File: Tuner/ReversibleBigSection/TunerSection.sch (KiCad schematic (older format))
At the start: 112 parts, among them J1 Conn_01x03, J10 Conn_01x02, J11 Conn_02x05_Odd_Even, J12 Conn_01x01, J13 Conn_01x01, J14 Conn_01x01, J15 Conn_01x01, J2 Conn_01x03, J3 Conn_01x03, J4 Conn_01x03, J5 Conn_01x03, J6 Conn_01x03, J7 Conn_01x03, J8 Conn_01x02, J9 Conn_01x02, P10 Conn_01x01, P11 Conn_01x01, P12 Conn_01x01, P2 Conn_01x01, P3 Conn_01x01, P4 Conn_01x01, P5 Conn_01x01, P6 Conn_01x01, P7 Conn_01x01, P8 Conn_01x01, P9 Conn_01x01, U1 MCP23008, U2 ULN2803A

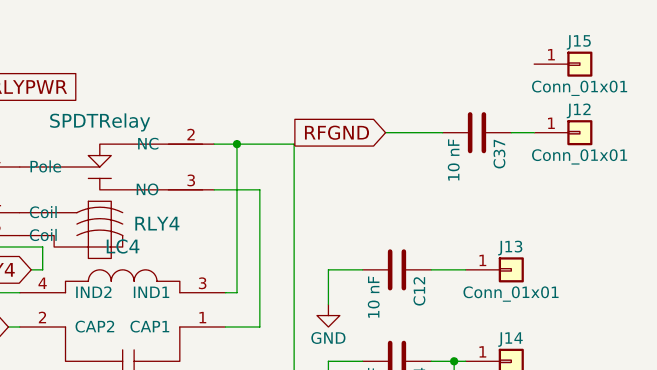
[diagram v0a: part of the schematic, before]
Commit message: Added HK19F boards
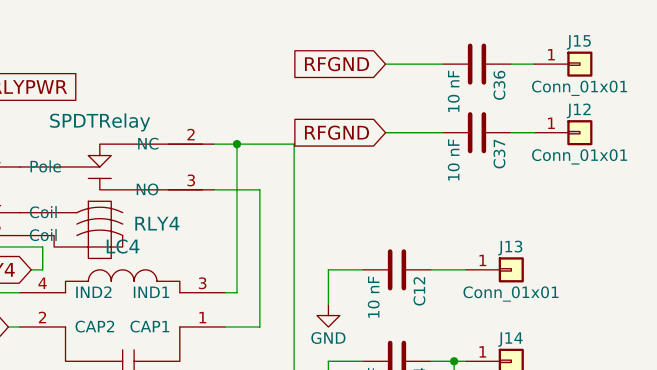
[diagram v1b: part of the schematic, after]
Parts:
- added C36: 10 nF, Capacitors_THT:C_Disc_D5.0mm_W2.5mm_P5.00mm, symbol C
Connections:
- net RFGND: now also C36.2
- net at J15.1 (Pin_1): now also C36.1
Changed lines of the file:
@@
 RLY8
 $Comp
-L +5V #PWR01
+L +5V #PWR13
 U 1 1 5B1A0287
 P 3150 5750
-F 0 "#PWR01" H 3150 5600 50  0001 C CNN
+F 0 "#PWR13" H 3150 5600 50  0001 C CNN
 F 1 "+5V" H 3150 5890 50  0000 C CNN
 F 2 "" H 3150 5750 50  0001 C CNN
@@
 $EndComp
 $Comp
-L GND #PWR02
+L GND #PWR3
 U 1 1 5B1AA0F6
 P 900 4500
-F 0 "#PWR02" H 900 4250 50  0001 C CNN
+F 0 "#PWR3" H 900 4250 50  0001 C CNN
 F 1 "GND" H 900 4350 50  0000 C CNN
 F 2 "" H 900 4500 50  0001 C CNN
@@
 $EndComp
 $Comp
-L +5V #PWR03
+L +5V #PWR2
 U 1 1 5B1AABE9
 P 900 3750
-F 0 "#PWR03" H 900 3600 50  0001 C CNN
+F 0 "#PWR2" H 900 3600 50  0001 C CNN
 F 1 "+5V" H 900 3890 50  0000 C CNN
 F 2 "" H 900 3750 50  0001 C CNN
@@
 $EndComp
 $Comp
-L +5V #PWR04
+L +5V #PWR9
 U 1 1 5B1ABA5A
 P 2150 4450
-F 0 "#PWR04" H 2150 4300 50  0001 C CNN
+F 0 "#PWR9" H 2150 4300 50  0001 C CNN
 F 1 "+5V" H 2150 4590 50  0000 C CNN
 F 2 "" H 2150 4450 50  0001 C CNN
@@
 $EndComp
 $Comp
-L +5V #PWR05
+L +5V #PWR11
 U 1 1 5B1ABCDE
 P 2400 3950
-F 0 "#PWR05" H 2400 3800 50  0001 C CNN
+F 0 "#PWR11" H 2400 3800 50  0001 C CNN
 F 1 "+5V" H 2400 4090 50  0000 C CNN
 F 2 "" H 2400 3950 50  0001 C CNN
@@
 $EndComp
 $Comp
-L +5V #PWR06
+L +5V #PWR17
 U 1 1 5B1ABFC6
 P 8800 4600
-F 0 "#PWR06" H 8800 4450 50  0001 C CNN
+F 0 "#PWR17" H 8800 4450 50  0001 C CNN
 F 1 "+5V" H 8800 4740 50  0000 C CNN
 F 2 "" H 8800 4600 50  0001 C CNN
@@
 $EndComp
 $Comp
-L GND #PWR07
+L GND #PWR18
 U 1 1 5B1AC04C
 P 8800 5050
-F 0 "#PWR07" H 8800 4800 50  0001 C CNN
+F 0 "#PWR18" H 8800 4800 50  0001 C CNN
 F 1 "GND" H 8800 4900 50  0000 C CNN
 F 2 "" H 8800 5050 50  0001 C CNN
@@
 $EndComp
 $Comp
-L +5V #PWR08
+L +5V #PWR10
 U 1 1 5B196BCE
 P 2250 3950
-F 0 "#PWR08" H 2250 3800 50  0001 C CNN
+F 0 "#PWR10" H 2250 3800 50  0001 C CNN
 F 1 "+5V" H 2250 4090 50  0000 C CNN
 F 2 "" H 2250 3950 50  0001 C CNN
@@
 $EndComp
 $Comp
-L GND #PWR09
+L GND #PWR15
 U 1 1 5B9A4AE1
 P 4850 6650
-F 0 "#PWR09" H 4850 6400 50  0001 C CNN
+F 0 "#PWR15" H 4850 6400 50  0001 C CNN
 F 1 "GND" H 4850 6500 50  0000 C CNN
 F 2 "" H 4850 6650 50  0001 C CNN
@@
 $EndComp
 $Comp
-L GND #PWR010
+L GND #PWR12
 U 1 1 5B9A6036
 P 3150 4200
-F 0 "#PWR010" H 3150 3950 50  0001 C CNN
+F 0 "#PWR12" H 3150 3950 50  0001 C CNN
 F 1 "GND" H 3150 4050 50  0000 C CNN
 F 2 "" H 3150 4200 50  0001 C CNN
@@
 $EndComp
 $Comp
-L GND #PWR011
+L GND #PWR14
 U 1 1 5B9ACA36
 P 3550 6100
-F 0 "#PWR011" H 3550 5850 50  0001 C CNN
+F 0 "#PWR14" H 3550 5850 50  0001 C CNN
 F 1 "GND" H 3550 5950 50  0000 C CNN
 F 2 "" H 3550 6100 50  0001 C CNN
@@
 $EndComp
 $Comp
-L GND #PWR012
+L GND #PWR19
 U 1 1 5B982525
 P 9850 2000
-F 0 "#PWR012" H 9850 1750 50  0001 C CNN
+F 0 "#PWR19" H 9850 1750 50  0001 C CNN
 F 1 "GND" H 9850 1850 50  0000 C CNN
 F 2 "" H 9850 2000 50  0001 C CNN
@@
 $EndComp
 $Comp
-L GND #PWR013
+L GND #PWR7
 U 1 1 5BA4D8F3
 P 1800 5850
-F 0 "#PWR013" H 1800 5600 50  0001 C CNN
+F 0 "#PWR7" H 1800 5600 50  0001 C CNN
 F 1 "GND" H 1800 5700 50  0000 C CNN
 F 2 "" H 1800 5850 50  0001 C CNN
@@
 $EndComp
 $Comp
-L +5V #PWR014
+L +5V #PWR8
 U 1 1 5BA4E273
 P 1850 5300
-F 0 "#PWR014" H 1850 5150 50  0001 C CNN
+F 0 "#PWR8" H 1850 5150 50  0001 C CNN
 F 1 "+5V" H 1850 5440 50  0000 C CNN
 F 2 "" H 1850 5300 50  0001 C CNN
@@
 $EndComp
 $Comp
-L +5V #PWR015
+L +5V #PWR6
 U 1 1 5BA4E663
 P 1200 5700
-F 0 "#PWR015" H 1200 5550 50  0001 C CNN
+F 0 "#PWR6" H 1200 5550 50  0001 C CNN
 F 1 "+5V" H 1200 5840 50  0000 C CNN
 F 2 "" H 1200 5700 50  0001 C CNN
@@
 $EndComp
 $Comp
-L GND #PWR016
+L GND #PWR1
 U 1 1 5BA4FB25
 P 750 5900
-F 0 "#PWR016" H 750 5650 50  0001 C CNN
+F 0 "#PWR1" H 750 5650 50  0001 C CNN
 F 1 "GND" H 750 5750 50  0000 C CNN
 F 2 "" H 750 5900 50  0001 C CNN
@@
 $EndComp
 $Comp
-L GND #PWR017
+L GND #PWR5
 U 1 1 5BA5005D
 P 1100 5300
-F 0 "#PWR017" H 1100 5050 50  0001 C CNN
+F 0 "#PWR5" H 1100 5050 50  0001 C CNN
 F 1 "GND" H 1100 5150 50  0000 C CNN
 F 2 "" H 1100 5300 50  0001 C CNN
@@
 EXTPWR
 $Comp
-L +5V #PWR018
+L +5V #PWR4
 U 1 1 5BAE4DBC
 P 1000 4850
-F 0 "#PWR018" H 1000 4700 50  0001 C CNN
+F 0 "#PWR4" H 1000 4700 50  0001 C CNN
 F 1 "+5V" H 1000 4990 50  0000 C CNN
 F 2 "" H 1000 4850 50  0001 C CNN
@@
 	700  4850 1000 4850
 $Comp
-L GND #PWR019
+L GND #PWR16
 U 1 1 5BAEE216
 P 5050 7250
-F 0 "#PWR019" H 5050 7000 50  0001 C CNN
+F 0 "#PWR16" H 5050 7000 50  0001 C CNN
 F 1 "GND" H 5050 7100 50  0000 C CNN
 F 2 "" H 5050 7250 50  0001 C CNN
@@
 Wire Wire Line
 	10100 1250 10350 1250
+$Comp
+L C C36
+U 1 1 5BCFC27C
+P 10500 950
+F 0 "C36" H 10525 1050 50  0000 L CNN
+F 1 "10 nF" H 10525 850 50  0000 L CNN
+F 2 "Capacitors_THT:C_Disc_D5.0mm_W2.5mm_P5.00mm" H 10538 800 50  0001 C CNN
+F 3 "" H 10500 950 50  0001 C CNN
+	1    10500 950
+	0    1    1    0
+$EndComp
+Text GLabel 10100 950  0    60   Input ~ 0
+RFGND
+Wire Wire Line
+	10100 950  10350 950
+Wire Wire Line
+	10650 950  10750 950
 $EndSCHEMATC

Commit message: JLCPCB Nov 1 2018
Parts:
- removed C36, C37: 10 nF, Capacitors_THT:C_Disc_D5.0mm_W2.5mm_P5.00mm, symbol C
- added J16, J17, J18, J19, J20, J21, J22: Conn_01x01, tuner:SOLDERJUMPER, symbol Conn_01x01
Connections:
- net RFGND: now also J17.1 (Pin_1)
- net at J9.2 (Pin_2), RLY9.2 (NC): now also J16.1 (Pin_1)
- net at J10.2 (Pin_2), RLY9.3 (NO): now also J22.1 (Pin_1)
- net at J15.1 (Pin_1): now also J18.1 (Pin_1), J19.1 (Pin_1)
- net at J12.1 (Pin_1): now also J20.1 (Pin_1), J21.1 (Pin_1)
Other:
- moved on the sheet: J12, J15
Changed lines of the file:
@@
 L Conn_01x01 J15
 U 1 1 5B19812D
-P 10950 950
-F 0 "J15" H 10950 1050 50  0000 C CNN
-F 1 "Conn_01x01" H 10950 850 50  0000 C CNN
-F 2 "Connectors:1pin" H 10950 950 50  0001 C CNN
-F 3 "" H 10950 950 50  0001 C CNN
-	1    10950 950
+P 11100 600
+F 0 "J15" H 11100 700 50  0000 C CNN
+F 1 "Conn_01x01" H 11100 500 50  0000 C CNN
+F 2 "Connectors:1pin" H 11100 600 50  0001 C CNN
+F 3 "" H 11100 600 50  0001 C CNN
+	1    11100 600
 	1    0    0    -1
 $EndComp
@@
 L Conn_01x01 J12
 U 1 1 5B1981D8
-P 10950 1250
-F 0 "J12" H 10950 1350 50  0000 C CNN
-F 1 "Conn_01x01" H 10950 1150 50  0000 C CNN
-F 2 "Connectors:1pin" H 10950 1250 50  0001 C CNN
-F 3 "" H 10950 1250 50  0001 C CNN
-	1    10950 1250
+P 11100 850
+F 0 "J12" H 11100 950 50  0000 C CNN
+F 1 "Conn_01x01" H 11100 750 50  0000 C CNN
+F 2 "Connectors:1pin" H 11100 850 50  0001 C CNN
+F 3 "" H 11100 850 50  0001 C CNN
+	1    11100 850
 	1    0    0    -1
 $EndComp
@@
 	-1   0    0    1
 $EndComp
+$Comp
+L GND #PWR16
+U 1 1 5BAEE216
+P 5050 7250
+F 0 "#PWR16" H 5050 7000 50  0001 C CNN
+F 1 "GND" H 5050 7100 50  0000 C CNN
+F 2 "" H 5050 7250 50  0001 C CNN
+F 3 "" H 5050 7250 50  0001 C CNN
+	1    5050 7250
+	1    0    0    -1
+$EndComp
+$Comp
+L C C34
+U 1 1 5BC6B88C
+P 5050 6000
+F 0 "C34" H 5075 6100 50  0000 L CNN
+F 1 "10 nF" H 5075 5900 50  0000 L CNN
+F 2 "Capacitors_THT:C_Disc_D5.0mm_W2.5mm_P5.00mm" H 5088 5850 50  0001 C CNN
+F 3 "" H 5050 6000 50  0001 C CNN
+	1    5050 6000
+	0    1    1    0
+$EndComp
+$Comp
+L C C35
+U 1 1 5BC6CF6F
+P 10150 2550
+F 0 "C35" H 10175 2650 50  0000 L CNN
+F 1 "10 nF" H 10175 2450 50  0000 L CNN
+F 2 "Capacitors_THT:C_Disc_D5.0mm_W2.5mm_P5.00mm" H 10188 2400 50  0001 C CNN
+F 3 "" H 10150 2550 50  0001 C CNN
+	1    10150 2550
+	0    1    1    0
+$EndComp
+Text GLabel 9600 650  0    60   Input ~ 0
+RFGND
+$Comp
+L Conn_01x01 J17
+U 1 1 5BD84E29
+P 9950 650
+F 0 "J17" H 9950 750 50  0000 C CNN
+F 1 "Conn_01x01" H 9950 550 50  0000 C CNN
+F 2 "tuner:SOLDERJUMPER" H 9950 650 50  0001 C CNN
+F 3 "" H 9950 650 50  0001 C CNN
+	1    9950 650
+	1    0    0    -1
+$EndComp
 Connection ~ 10200 5350
 Wire Wire Line
@@
 	10150 4150 10150 3700
 Wire Wire Line
-	9600 4150 10150 4150
+	9600 4150 10350 4150
 Wire Wire Line
 	9900 3200 10150 3200
@@
 Wire Wire Line
 	700  4850 1000 4850
-$Comp
-L GND #PWR16
-U 1 1 5BAEE216
-P 5050 7250
-F 0 "#PWR16" H 5050 7000 50  0001 C CNN
-F 1 "GND" H 5050 7100 50  0000 C CNN
-F 2 "" H 5050 7250 50  0001 C CNN
-F 3 "" H 5050 7250 50  0001 C CNN
-	1    5050 7250
-	1    0    0    -1
-$EndComp
 Wire Wire Line
 	5050 7200 5050 7250
@@
 	5050 6600 5250 6600
 Connection ~ 5250 6600
-$Comp
-L C C34
-U 1 1 5BC6B88C
-P 5050 6000
-F 0 "C34" H 5075 6100 50  0000 L CNN
-F 1 "10 nF" H 5075 5900 50  0000 L CNN
-F 2 "Capacitors_THT:C_Disc_D5.0mm_W2.5mm_P5.00mm" H 5088 5850 50  0001 C CNN
-F 3 "" H 5050 6000 50  0001 C CNN
-	1    5050 6000
-	0    1    1    0
-$EndComp
 Wire Wire Line
 	4700 6000 4900 6000
@@
 	5250 6000 5200 6000
 Connection ~ 5250 6000
-$Comp
-L C C35
-U 1 1 5BC6CF6F
-P 10150 2550
-F 0 "C35" H 10175 2650 50  0000 L CNN
-F 1 "10 nF" H 10175 2450 50  0000 L CNN
-F 2 "Capacitors_THT:C_Disc_D5.0mm_W2.5mm_P5.00mm" H 10188 2400 50  0001 C CNN
-F 3 "" H 10150 2550 50  0001 C CNN
-	1    10150 2550
-	0    1    1    0
-$EndComp
 Wire Wire Line
 	9850 2550 10000 2550
@@
 	10400 2550 10400 2250
 Connection ~ 10400 2250
-Text GLabel 10100 1250 0    60   Input ~ 0
-RFGND
-$Comp
-L C C37
-U 1 1 5BCC2C84
-P 10500 1250
-F 0 "C37" H 10525 1350 50  0000 L CNN
-F 1 "10 nF" H 10525 1150 50  0000 L CNN
-F 2 "Capacitors_THT:C_Disc_D5.0mm_W2.5mm_P5.00mm" H 10538 1100 50  0001 C CNN
-F 3 "" H 10500 1250 50  0001 C CNN
-	1    10500 1250
-	0    1    1    0
-$EndComp
-Wire Wire Line
-	10650 1250 10750 1250
-Wire Wire Line
-	10100 1250 10350 1250
-$Comp
-L C C36
-U 1 1 5BCFC27C
-P 10500 950
-F 0 "C36" H 10525 1050 50  0000 L CNN
-F 1 "10 nF" H 10525 850 50  0000 L CNN
-F 2 "Capacitors_THT:C_Disc_D5.0mm_W2.5mm_P5.00mm" H 10538 800 50  0001 C CNN
-F 3 "" H 10500 950 50  0001 C CNN
-	1    10500 950
-	0    1    1    0
-$EndComp
-Text GLabel 10100 950  0    60   Input ~ 0
-RFGND
-Wire Wire Line
-	10100 950  10350 950
-Wire Wire Line
-	10650 950  10750 950
+Wire Wire Line
+	9750 650  9600 650
+$Comp
+L Conn_01x01 J18
+U 1 1 5BD85A19
+P 10550 550
+F 0 "J18" H 10550 650 50  0000 C CNN
+F 1 "Conn_01x01" H 10550 450 50  0000 C CNN
+F 2 "tuner:SOLDERJUMPER" H 10550 550 50  0001 C CNN
+F 3 "" H 10550 550 50  0001 C CNN
+	1    10550 550
+	-1   0    0    1
+$EndComp
+$Comp
+L Conn_01x01 J19
+U 1 1 5BD85C02
+P 10550 650
+F 0 "J19" H 10550 750 50  0000 C CNN
+F 1 "Conn_01x01" H 10550 550 50  0000 C CNN
+F 2 "tuner:SOLDERJUMPER" H 10550 650 50  0001 C CNN
+F 3 "" H 10550 650 50  0001 C CNN
+	1    10550 650
+	-1   0    0    1
+$EndComp
+Wire Wire Line
+	10750 550  10750 650
+Wire Wire Line
+	10750 600  10900 600
+Connection ~ 10750 600
+$Comp
+L Conn_01x01 J20
+U 1 1 5BD861F6
+P 10550 850
+F 0 "J20" H 10550 950 50  0000 C CNN
+F 1 "Conn_01x01" H 10550 750 50  0000 C CNN
+F 2 "tuner:SOLDERJUMPER" H 10550 850 50  0001 C CNN
+F 3 "" H 10550 850 50  0001 C CNN
+	1    10550 850
+	-1   0    0    1
+$EndComp
+$Comp
+L Conn_01x01 J21
+U 1 1 5BD86365
+P 10550 950
+F 0 "J21" H 10550 1050 50  0000 C CNN
+F 1 "Conn_01x01" H 10550 850 50  0000 C CNN
+F 2 "tuner:SOLDERJUMPER" H 10550 950 50  0001 C CNN
+F 3 "" H 10550 950 50  0001 C CNN
+	1    10550 950
+	-1   0    0    1
+$EndComp
+Wire Wire Line
+	10750 850  10750 950
+Wire Wire Line
+	10900 850  10900 900
+Wire Wire Line
+	10900 900  10750 900
+Connection ~ 10750 900
+$Comp
+L Conn_01x01 J22
+U 1 1 5BD86A55
+P 10550 4150
+F 0 "J22" H 10550 4250 50  0000 C CNN
+F 1 "Conn_01x01" H 10550 4050 50  0000 C CNN
+F 2 "tuner:SOLDERJUMPER" H 10550 4150 50  0001 C CNN
+F 3 "" H 10550 4150 50  0001 C CNN
+	1    10550 4150
+	1    0    0    -1
+$EndComp
+Connection ~ 10150 4150
+$Comp
+L Conn_01x01 J16
+U 1 1 5BD872C1
+P 9550 3750
+F 0 "J16" H 9550 3850 50  0000 C CNN
+F 1 "Conn_01x01" H 9550 3650 50  0000 C CNN
+F 2 "tuner:SOLDERJUMPER" H 9550 3750 50  0001 C CNN
+F 3 "" H 9550 3750 50  0001 C CNN
+	1    9550 3750
+	-1   0    0    1
+$EndComp
+Wire Wire Line
+	9750 3750 9900 3750
+Connection ~ 9900 3750
 $EndSCHEMATC

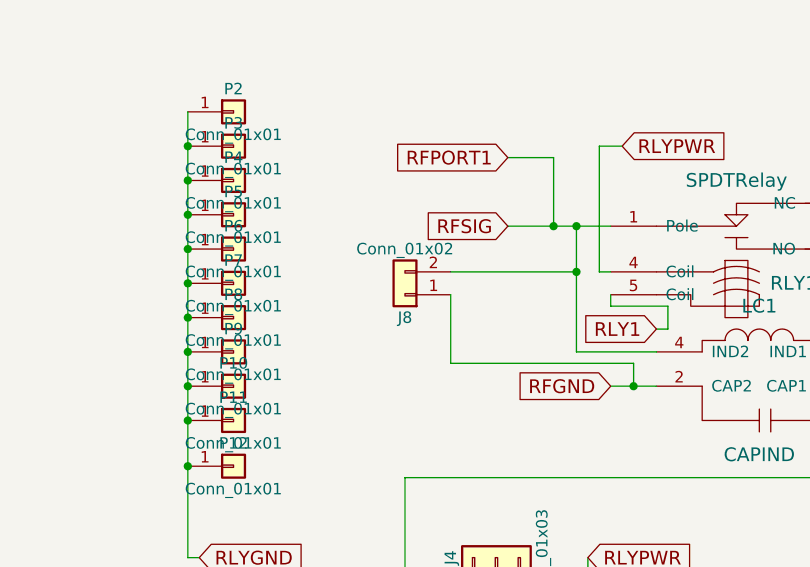
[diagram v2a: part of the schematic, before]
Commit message: Modified connectors on Reversible boards
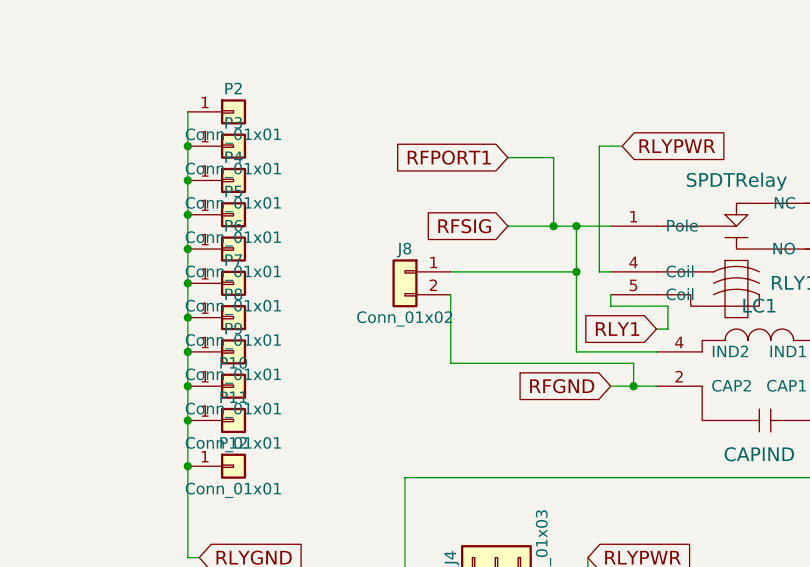
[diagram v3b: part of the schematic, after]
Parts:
- J10, J8, J9: footprint Connectors_Terminal_Blocks:TerminalBlock_bornier-2_P5.08mm -> tuner:bnc_90_1-1337543-0_pad_combo
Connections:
- net RFGND: now also J8.2 (Pin_2); no longer J8.1 (Pin_1)
- net RFPORT1: now also J8.1 (Pin_1); no longer J8.2 (Pin_2)
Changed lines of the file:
@@
 L Conn_01x02 J8
 U 1 1 5B18E79B
-P 2150 1700
-F 0 "J8" H 2150 1800 50  0000 C CNN
-F 1 "Conn_01x02" H 2150 1500 50  0000 C CNN
-F 2 "Connectors_Terminal_Blocks:TerminalBlock_bornier-2_P5.08mm" H 2150 1700 50  0001 C CNN
-F 3 "" H 2150 1700 50  0001 C CNN
-	1    2150 1700
-	-1   0    0    1
+P 2150 1600
+F 0 "J8" H 2150 1700 50  0000 C CNN
+F 1 "Conn_01x02" H 2150 1400 50  0000 C CNN
+F 2 "tuner:bnc_90_1-1337543-0_pad_combo" H 2150 1600 50  0001 C CNN
+F 3 "" H 2150 1600 50  0001 C CNN
+	1    2150 1600
+	-1   0    0    -1
 $EndComp
 $Comp
@@
 F 0 "J10" H 10350 3700 50  0000 C CNN
 F 1 "Conn_01x02" H 10350 3400 50  0000 C CNN
-F 2 "Connectors_Terminal_Blocks:TerminalBlock_bornier-2_P5.08mm" H 10350 3600 50  0001 C CNN
+F 2 "tuner:bnc_90_1-1337543-0_pad_combo" H 10350 3600 50  0001 C CNN
 F 3 "" H 10350 3600 50  0001 C CNN
 	1    10350 3600
@@
 RLY8
 $Comp
-L +5V #PWR13
+L +5V #PWR01
 U 1 1 5B1A0287
 P 3150 5750
-F 0 "#PWR13" H 3150 5600 50  0001 C CNN
+F 0 "#PWR01" H 3150 5600 50  0001 C CNN
 F 1 "+5V" H 3150 5890 50  0000 C CNN
 F 2 "" H 3150 5750 50  0001 C CNN
@@
 $EndComp
 $Comp
-L GND #PWR3
+L GND #PWR02
 U 1 1 5B1AA0F6
 P 900 4500
-F 0 "#PWR3" H 900 4250 50  0001 C CNN
+F 0 "#PWR02" H 900 4250 50  0001 C CNN
 F 1 "GND" H 900 4350 50  0000 C CNN
 F 2 "" H 900 4500 50  0001 C CNN
@@
 $EndComp
 $Comp
-L +5V #PWR2
+L +5V #PWR03
 U 1 1 5B1AABE9
 P 900 3750
-F 0 "#PWR2" H 900 3600 50  0001 C CNN
+F 0 "#PWR03" H 900 3600 50  0001 C CNN
 F 1 "+5V" H 900 3890 50  0000 C CNN
 F 2 "" H 900 3750 50  0001 C CNN
@@
 $EndComp
 $Comp
-L +5V #PWR9
+L +5V #PWR04
 U 1 1 5B1ABA5A
 P 2150 4450
-F 0 "#PWR9" H 2150 4300 50  0001 C CNN
+F 0 "#PWR04" H 2150 4300 50  0001 C CNN
 F 1 "+5V" H 2150 4590 50  0000 C CNN
 F 2 "" H 2150 4450 50  0001 C CNN
@@
 $EndComp
 $Comp
-L +5V #PWR11
+L +5V #PWR05
 U 1 1 5B1ABCDE
 P 2400 3950
-F 0 "#PWR11" H 2400 3800 50  0001 C CNN
+F 0 "#PWR05" H 2400 3800 50  0001 C CNN
 F 1 "+5V" H 2400 4090 50  0000 C CNN
 F 2 "" H 2400 3950 50  0001 C CNN
@@
 $EndComp
 $Comp
-L +5V #PWR17
+L +5V #PWR06
 U 1 1 5B1ABFC6
 P 8800 4600
-F 0 "#PWR17" H 8800 4450 50  0001 C CNN
+F 0 "#PWR06" H 8800 4450 50  0001 C CNN
 F 1 "+5V" H 8800 4740 50  0000 C CNN
 F 2 "" H 8800 4600 50  0001 C CNN
@@
 $EndComp
 $Comp
-L GND #PWR18
+L GND #PWR07
 U 1 1 5B1AC04C
 P 8800 5050
-F 0 "#PWR18" H 8800 4800 50  0001 C CNN
+F 0 "#PWR07" H 8800 4800 50  0001 C CNN
 F 1 "GND" H 8800 4900 50  0000 C CNN
 F 2 "" H 8800 5050 50  0001 C CNN
@@
 F 0 "J9" H 10350 3200 50  0000 C CNN
 F 1 "Conn_01x02" H 10350 2900 50  0000 C CNN
-F 2 "Connectors_Terminal_Blocks:TerminalBlock_bornier-2_P5.08mm" H 10350 3100 50  0001 C CNN
+F 2 "tuner:bnc_90_1-1337543-0_pad_combo" H 10350 3100 50  0001 C CNN
 F 3 "" H 10350 3100 50  0001 C CNN
 	1    10350 3100
@@
 $EndComp
 $Comp
-L +5V #PWR10
+L +5V #PWR08
 U 1 1 5B196BCE
 P 2250 3950
-F 0 "#PWR10" H 2250 3800 50  0001 C CNN
+F 0 "#PWR08" H 2250 3800 50  0001 C CNN
 F 1 "+5V" H 2250 4090 50  0000 C CNN
 F 2 "" H 2250 3950 50  0001 C CNN
@@
 $EndComp
 $Comp
-L GND #PWR15
+L GND #PWR09
 U 1 1 5B9A4AE1
 P 4850 6650
-F 0 "#PWR15" H 4850 6400 50  0001 C CNN
+F 0 "#PWR09" H 4850 6400 50  0001 C CNN
 F 1 "GND" H 4850 6500 50  0000 C CNN
 F 2 "" H 4850 6650 50  0001 C CNN
@@
 $EndComp
 $Comp
-L GND #PWR12
+L GND #PWR010
 U 1 1 5B9A6036
 P 3150 4200
-F 0 "#PWR12" H 3150 3950 50  0001 C CNN
+F 0 "#PWR010" H 3150 3950 50  0001 C CNN
 F 1 "GND" H 3150 4050 50  0000 C CNN
 F 2 "" H 3150 4200 50  0001 C CNN
@@
 $EndComp
 $Comp
-L GND #PWR14
+L GND #PWR011
 U 1 1 5B9ACA36
 P 3550 6100
-F 0 "#PWR14" H 3550 5850 50  0001 C CNN
+F 0 "#PWR011" H 3550 5850 50  0001 C CNN
 F 1 "GND" H 3550 5950 50  0000 C CNN
 F 2 "" H 3550 6100 50  0001 C CNN
@@
 $EndComp
 $Comp
-L GND #PWR19
+L GND #PWR012
 U 1 1 5B982525
 P 9850 2000
-F 0 "#PWR19" H 9850 1750 50  0001 C CNN
+F 0 "#PWR012" H 9850 1750 50  0001 C CNN
 F 1 "GND" H 9850 1850 50  0000 C CNN
 F 2 "" H 9850 2000 50  0001 C CNN
@@
 $EndComp
 $Comp
-L GND #PWR7
+L GND #PWR013
 U 1 1 5BA4D8F3
 P 1800 5850
-F 0 "#PWR7" H 1800 5600 50  0001 C CNN
+F 0 "#PWR013" H 1800 5600 50  0001 C CNN
 F 1 "GND" H 1800 5700 50  0000 C CNN
 F 2 "" H 1800 5850 50  0001 C CNN
@@
 $EndComp
 $Comp
-L +5V #PWR8
+L +5V #PWR014
 U 1 1 5BA4E273
 P 1850 5300
-F 0 "#PWR8" H 1850 5150 50  0001 C CNN
+F 0 "#PWR014" H 1850 5150 50  0001 C CNN
 F 1 "+5V" H 1850 5440 50  0000 C CNN
 F 2 "" H 1850 5300 50  0001 C CNN
@@
 $EndComp
 $Comp
-L +5V #PWR6
+L +5V #PWR015
 U 1 1 5BA4E663
 P 1200 5700
-F 0 "#PWR6" H 1200 5550 50  0001 C CNN
+F 0 "#PWR015" H 1200 5550 50  0001 C CNN
 F 1 "+5V" H 1200 5840 50  0000 C CNN
 F 2 "" H 1200 5700 50  0001 C CNN
@@
 $EndComp
 $Comp
-L GND #PWR1
+L GND #PWR016
 U 1 1 5BA4FB25
 P 750 5900
-F 0 "#PWR1" H 750 5650 50  0001 C CNN
+F 0 "#PWR016" H 750 5650 50  0001 C CNN
 F 1 "GND" H 750 5750 50  0000 C CNN
 F 2 "" H 750 5900 50  0001 C CNN
@@
 $EndComp
 $Comp
-L GND #PWR5
+L GND #PWR017
 U 1 1 5BA5005D
 P 1100 5300
-F 0 "#PWR5" H 1100 5050 50  0001 C CNN
+F 0 "#PWR017" H 1100 5050 50  0001 C CNN
 F 1 "GND" H 1100 5150 50  0000 C CNN
 F 2 "" H 1100 5300 50  0001 C CNN
@@
 EXTPWR
 $Comp
-L +5V #PWR4
+L +5V #PWR018
 U 1 1 5BAE4DBC
 P 1000 4850
-F 0 "#PWR4" H 1000 4700 50  0001 C CNN
+F 0 "#PWR018" H 1000 4700 50  0001 C CNN
 F 1 "+5V" H 1000 4990 50  0000 C CNN
 F 2 "" H 1000 4850 50  0001 C CNN
@@
 $EndComp
 $Comp
-L GND #PWR16
+L GND #PWR019
 U 1 1 5BAEE216
 P 5050 7250
-F 0 "#PWR16" H 5050 7000 50  0001 C CNN
+F 0 "#PWR019" H 5050 7000 50  0001 C CNN
 F 1 "GND" H 5050 7100 50  0000 C CNN
 F 2 "" H 5050 7250 50  0001 C CNN
